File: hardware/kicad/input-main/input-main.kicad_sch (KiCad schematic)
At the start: 0 parts

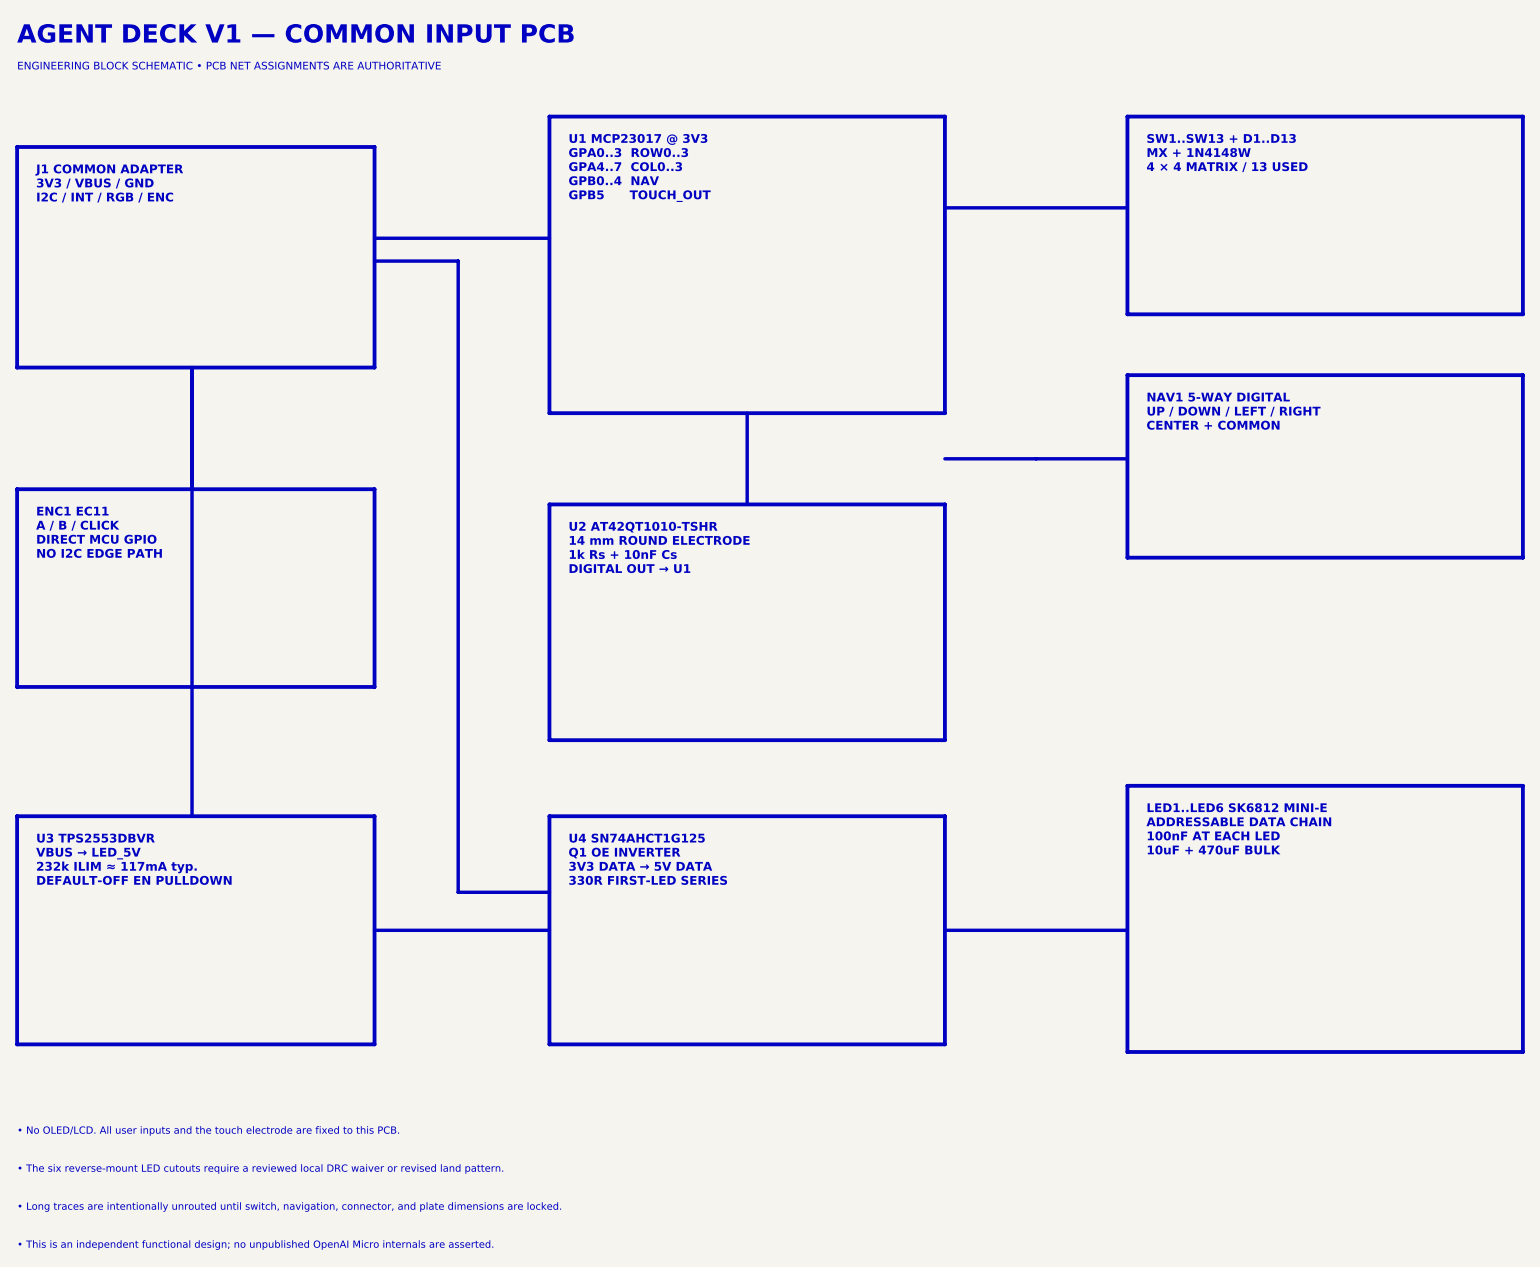
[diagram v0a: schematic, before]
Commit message: Let every control key communicate agent state without more MCU pins
Constraint: Preserve RGB_DATA and RGB_PWR_EN allocation and the provisional 120 mA aggregate budget
Rejected: Raise the hardware current limit now | Optical, USB-budget, transient, and thermal measurements are not available
Confidence: high
Scope-risk: moderate
Directive: Do not increase RGB current or release Gerbers until the 13-key optical stack and all-white clamp tests pass
Tested: KiCad generator completed; LED1-LED13 chain and C1-C13 asserted; all three schematic ERCs report 0; renders inspected; DRC debt recorded
Not-tested: Physical keycap illumination, full routing, touch-noise immunity, thermal behavior, and first-article current
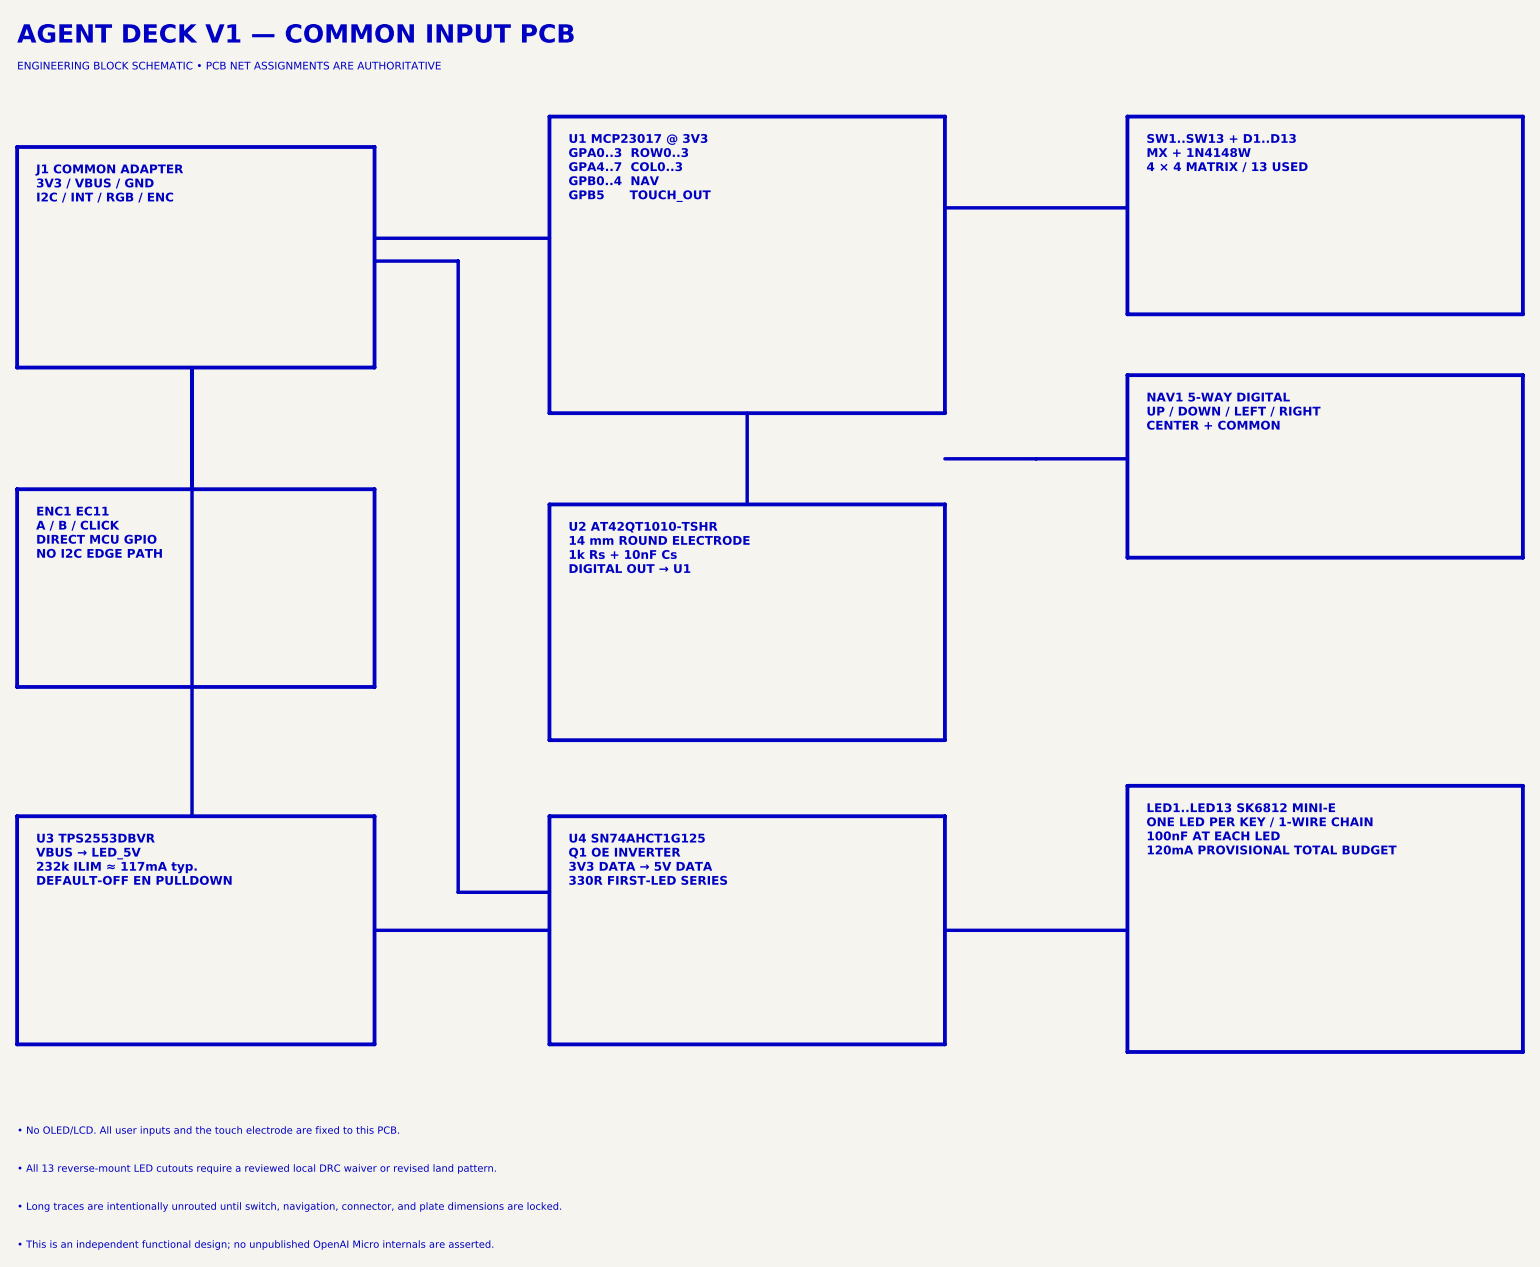
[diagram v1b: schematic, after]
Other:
- note added: "LED1..LED13 SK6812 MINI-E ONE LED PER KEY / 1-WIRE CHAIN 100nF AT EACH LED 120mA PROVISIONAL TOTAL BUDGET"
- note added: "• All 13 reverse-mount LED cutouts require a reviewed local DRC waiver or revised land pattern."
- note removed: "LED1..LED6 SK6812 MINI-E ADDRESSABLE DATA CHAIN 100nF AT EACH LED 10uF + 470uF BULK"
- note removed: "• The six reverse-mount LED cutouts require a reviewed local DRC waiver or revised land pattern."
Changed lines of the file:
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@@
 		(stroke (width 0.500) (type solid))
 	)
-	(text "LED1..LED6 SK6812 MINI-E\nADDRESSABLE DATA CHAIN\n100nF AT EACH LED\n10uF + 470uF BULK"
+	(text "LED1..LED13 SK6812 MINI-E\nONE LED PER KEY / 1-WIRE CHAIN\n100nF AT EACH LED\n120mA PROVISIONAL TOTAL BUDGET"
 		(exclude_from_sim no)
 		(at 166.500 114.500 0)
@@
 		)
 	)
-	(text "• The six reverse-mount LED cutouts require a reviewed local DRC waiver or revised land pattern."
+	(text "• All 13 reverse-mount LED cutouts require a reviewed local DRC waiver or revised land pattern."
 		(exclude_from_sim no)
 		(at 18.000 162.000 0)

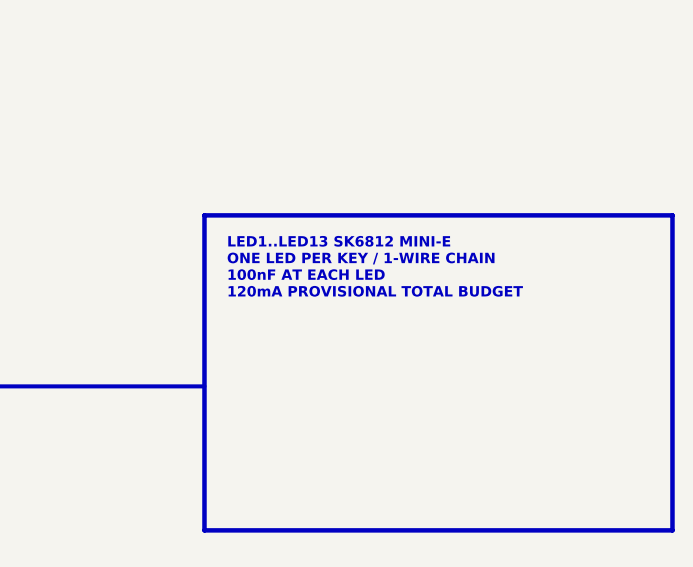
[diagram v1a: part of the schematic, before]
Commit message: Make the physical control surface serviceable and printable
Constraint: Preserve an independent public-exterior reference without asserting unpublished OpenAI Micro internals.
Rejected: Soldered switches, a square navigation cap, a tall radial bulk capacitor, and the isolated lower-right K13 placement.
Confidence: high
Scope-risk: broad
Directive: Keep this revision out of fabrication until socket, navigation, touch, USB, battery, and first-article fit gates pass.
Tested: KiCad 10.0.4 ERC on all projects; DRC with no short, copper-clearance, hole-clearance, or crossing findings; 13-key/13-LED geometry assertions; Blender 5.1.2 manifold STL generation and visual render review.
Not-tested: Physical switch/socket/joystick samples, printed fit, touch sensitivity, USB cable access, battery fit, antenna performance, or assembled electrical operation.
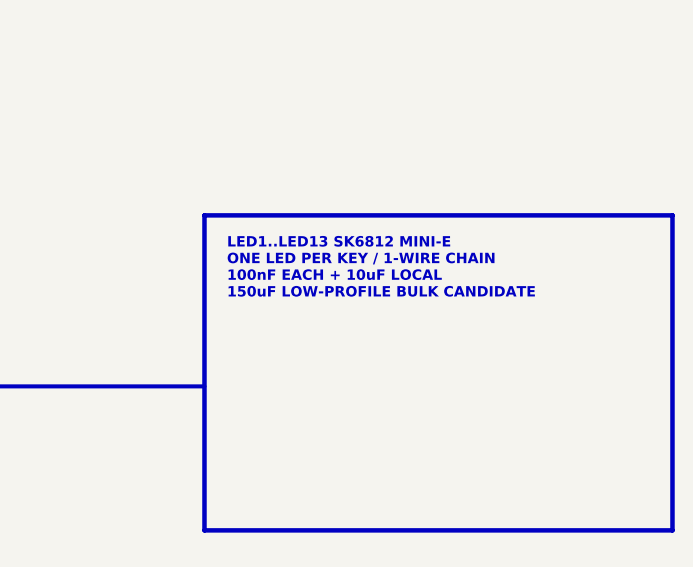
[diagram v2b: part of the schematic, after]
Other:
- note added: "LED1..LED13 SK6812 MINI-E ONE LED PER KEY / 1-WIRE CHAIN 100nF EACH + 10uF LOCAL 150uF LOW-PROFILE BULK CANDIDATE"
- note removed: "LED1..LED13 SK6812 MINI-E ONE LED PER KEY / 1-WIRE CHAIN 100nF AT EACH LED 120mA PROVISIONAL TOTAL BUDGET"
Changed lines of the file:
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@@
 		(stroke (width 0.500) (type solid))
 	)
-	(text "LED1..LED13 SK6812 MINI-E\nONE LED PER KEY / 1-WIRE CHAIN\n100nF AT EACH LED\n120mA PROVISIONAL TOTAL BUDGET"
+	(text "LED1..LED13 SK6812 MINI-E\nONE LED PER KEY / 1-WIRE CHAIN\n100nF EACH + 10uF LOCAL\n150uF LOW-PROFILE BULK CANDIDATE"
 		(exclude_from_sim no)
 		(at 166.500 114.500 0)

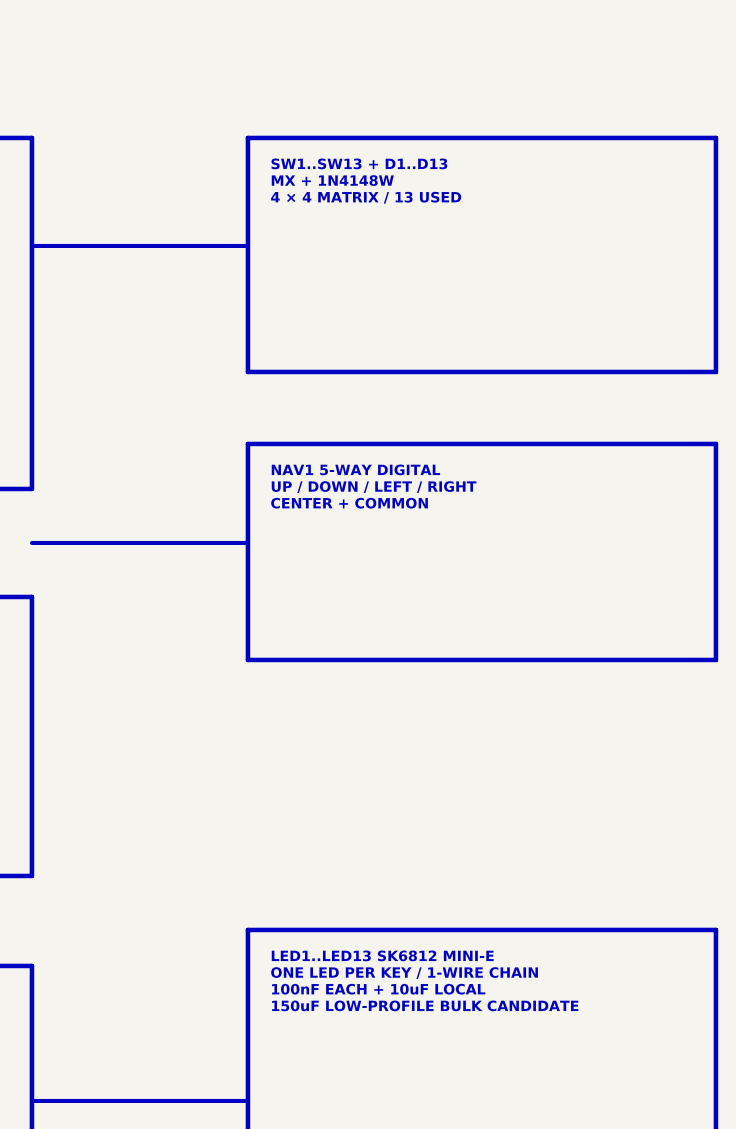
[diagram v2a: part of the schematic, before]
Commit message: Align the physical controls with the observable Codex layout
The square controller now uses twelve hot-swap MX keys so the upper-right position belongs to the navigation control, while K11 remains a wide host-side push-to-talk control.

Constraint: Preserve independent circuitry and avoid claims about unpublished Codex Micro internals

Rejected: Keep a thirteenth MX key in the top row | it displaced the joystick from the observable layout

Confidence: high

Scope-risk: moderate

Directive: Add K11 stabilizer geometry only from the selected part drawing before fabrication

Tested: KiCad ERC on three projects; KiCad DRC and renders on three boards; Blender manifold checks and top-view visual inspection; BOM/JSON parsing; git diff check

Not-tested: Physical fit, touch sensitivity, stabilizer samples, and intentionally open release routing
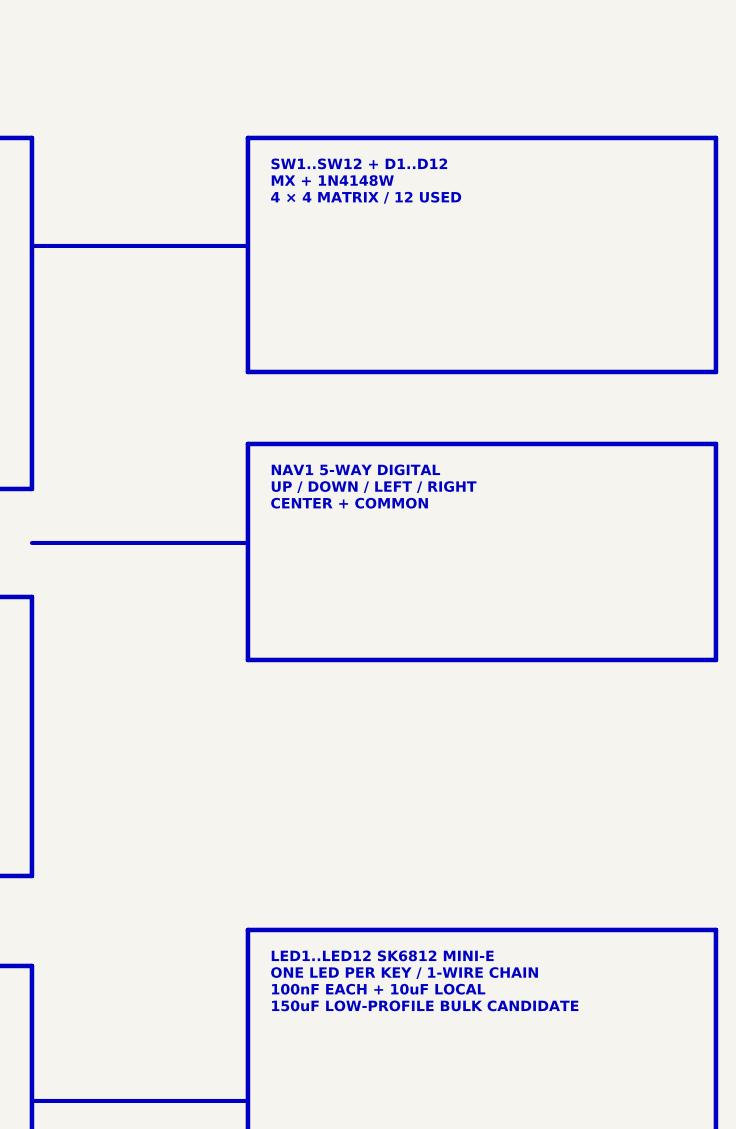
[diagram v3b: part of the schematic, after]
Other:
- note added: "LED1..LED12 SK6812 MINI-E ONE LED PER KEY / 1-WIRE CHAIN 100nF EACH + 10uF LOCAL 150uF LOW-PROFILE BULK CANDIDATE"
- note added: "SW1..SW12 + D1..D12 MX + 1N4148W 4 × 4 MATRIX / 12 USED"
- note removed: "LED1..LED13 SK6812 MINI-E ONE LED PER KEY / 1-WIRE CHAIN 100nF EACH + 10uF LOCAL 150uF LOW-PROFILE BULK CANDIDATE"
- note removed: "SW1..SW13 + D1..D13 MX + 1N4148W 4 × 4 MATRIX / 13 USED"
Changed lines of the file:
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@@
 		(stroke (width 0.500) (type solid))
 	)
-	(text "SW1..SW13 + D1..D13\nMX + 1N4148W\n4 × 4 MATRIX / 13 USED"
+	(text "SW1..SW12 + D1..D12\nMX + 1N4148W\n4 × 4 MATRIX / 12 USED"
 		(exclude_from_sim no)
 		(at 166.500 26.500 0)
@@
 		(stroke (width 0.500) (type solid))
 	)
-	(text "LED1..LED13 SK6812 MINI-E\nONE LED PER KEY / 1-WIRE CHAIN\n100nF EACH + 10uF LOCAL\n150uF LOW-PROFILE BULK CANDIDATE"
+	(text "LED1..LED12 SK6812 MINI-E\nONE LED PER KEY / 1-WIRE CHAIN\n100nF EACH + 10uF LOCAL\n150uF LOW-PROFILE BULK CANDIDATE"
 		(exclude_from_sim no)
 		(at 166.500 114.500 0)

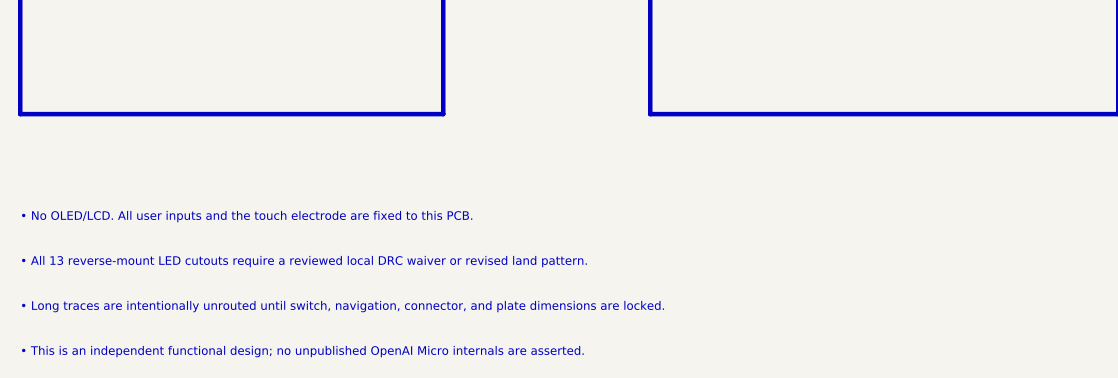
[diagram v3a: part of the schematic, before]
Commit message: Establish a host-verified V1 baseline before physical bring-up
Constraint: The common PCB remains 100 mm square, all controls stay PCB-mounted, and no display is added.
Rejected: Deterministic adapter autorouting | KiCad exposed real escape and via conflicts, so reviewed manual routing remains explicit.
Confidence: medium
Scope-risk: broad
Directive: Do not order boards until all open connections are routed, complete schematics pass parity, exact parts pass sample fit, and physical power/RF/USB/BLE tests succeed.
Tested: KiCad block ERC 0 on three projects; DRC 0 errors with documented warnings and open nets; Blender manifold STL generation; firmware 12/12 normal, sanitized, and embedded-style builds; bridge 41/41 on Python 3.11 and 3.14.
Not-tested: Physical XIAO USB/BLE, RF, battery charging and swelling, touch sensitivity, connector mating, real audio backend, and assembled endurance.
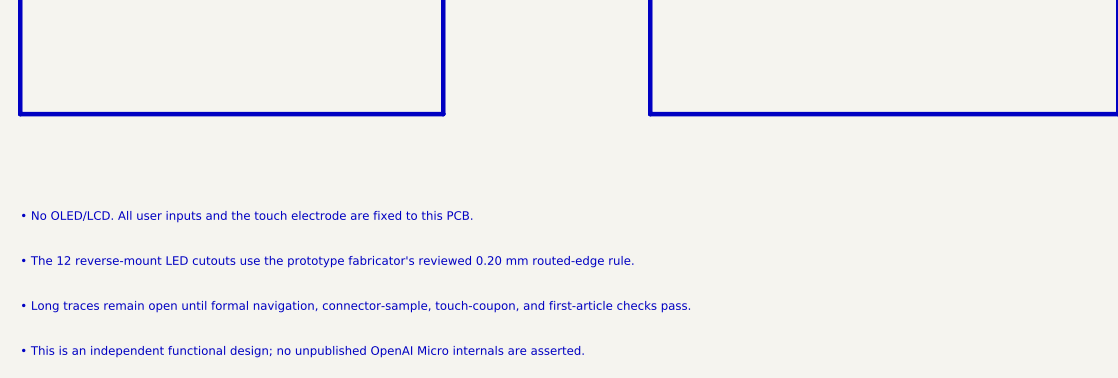
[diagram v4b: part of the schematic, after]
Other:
- note added: "• Long traces remain open until formal navigation, connector-sample, touch-coupon, and first-article checks pass."
- note added: "• The 12 reverse-mount LED cutouts use the prototype fabricator's reviewed 0.20 mm routed-edge rule."
- note removed: "• All 13 reverse-mount LED cutouts require a reviewed local DRC waiver or revised land pattern."
- note removed: "• Long traces are intentionally unrouted until switch, navigation, connector, and plate dimensions are locked."
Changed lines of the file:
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@@
 		)
 	)
-	(text "• All 13 reverse-mount LED cutouts require a reviewed local DRC waiver or revised land pattern."
+	(text "• The 12 reverse-mount LED cutouts use the prototype fabricator's reviewed 0.20 mm routed-edge rule."
 		(exclude_from_sim no)
 		(at 18.000 162.000 0)
@@
 		)
 	)
-	(text "• Long traces are intentionally unrouted until switch, navigation, connector, and plate dimensions are locked."
+	(text "• Long traces remain open until formal navigation, connector-sample, touch-coupon, and first-article checks pass."
 		(exclude_from_sim no)
 		(at 18.000 167.000 0)
